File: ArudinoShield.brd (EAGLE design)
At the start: 53.3 x 60.6 mm, 25 parts, among them IC1 L298

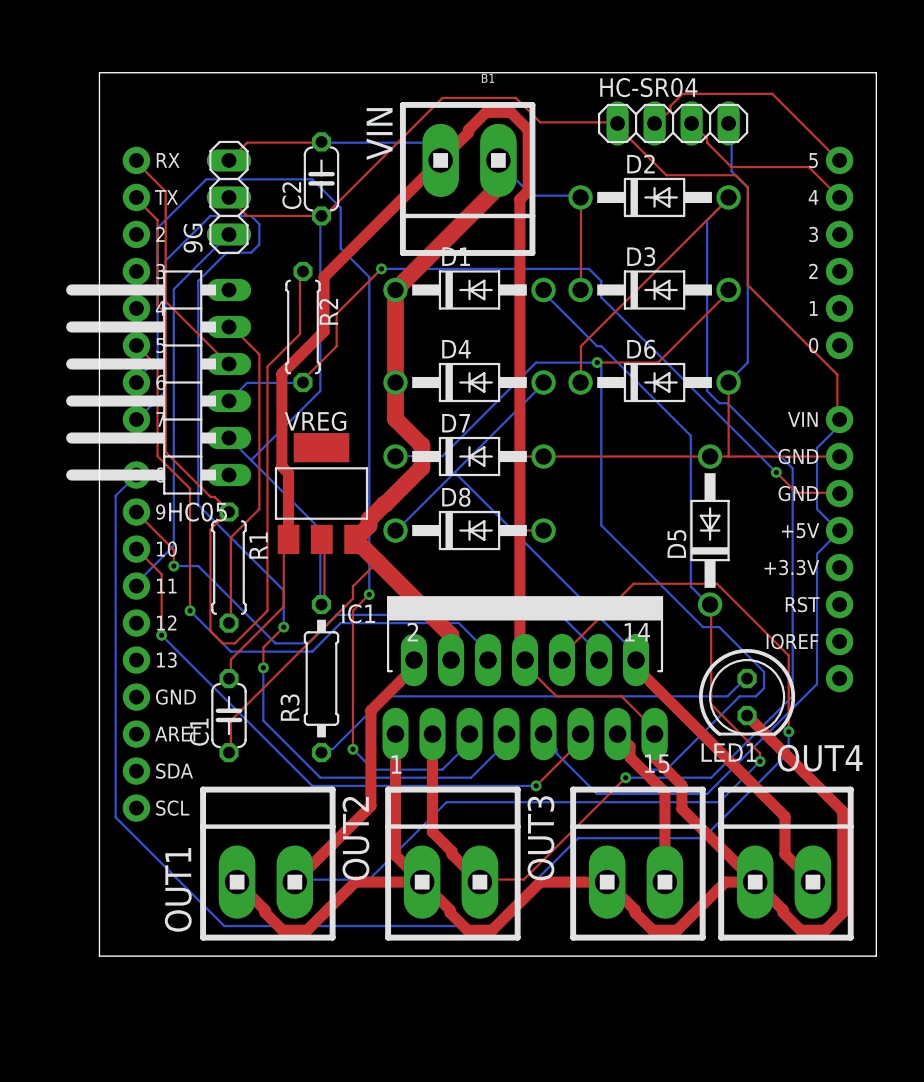
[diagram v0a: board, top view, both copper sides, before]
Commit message: added ground plane, updated layout
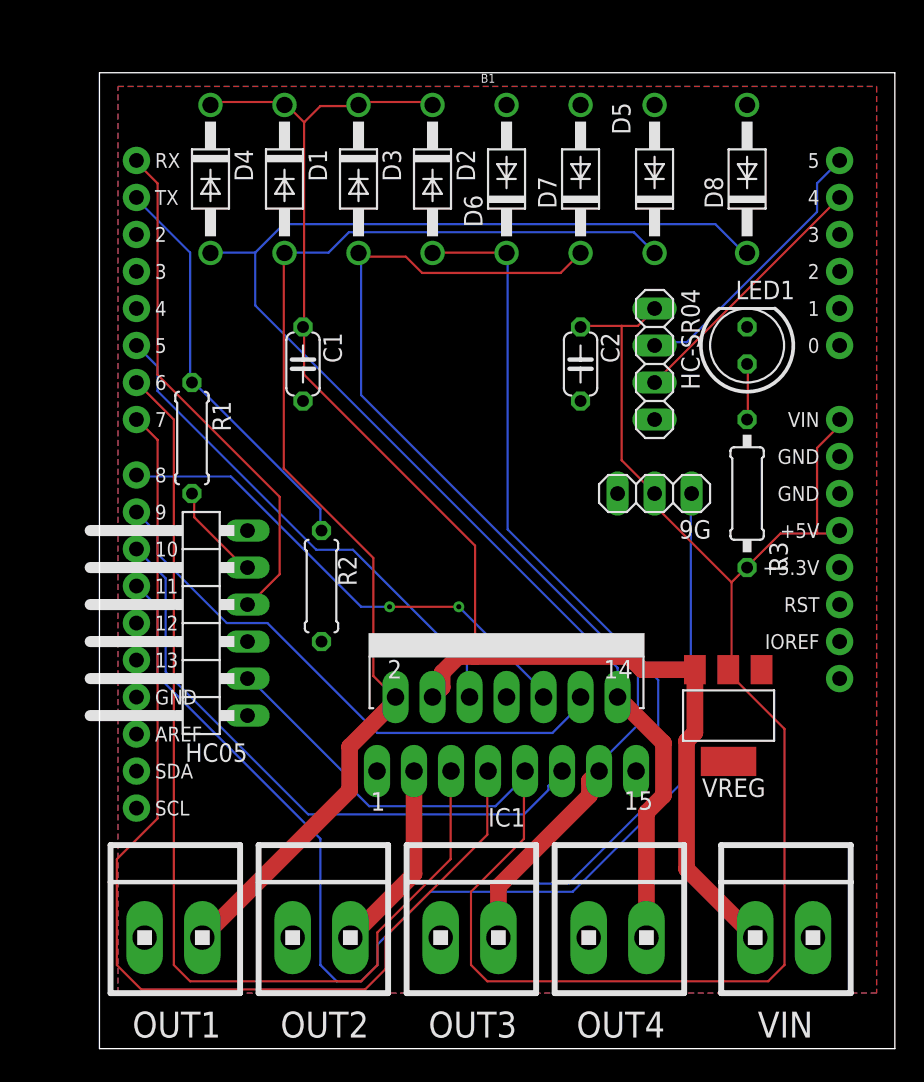
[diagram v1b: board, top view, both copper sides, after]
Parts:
- moved VIN 57.5 mm to (81.3, 20.3), turned to 0 degrees
- moved 9G 35.6 mm to (72.4, 50.8), turned to 180 degrees
- moved R3 31.9 mm to (78.7, 50.8), turned to 270 degrees
- moved VREG 31.8 mm to (77.5, 35.6), turned to 180 degrees
- moved D8 30.7 mm to (78.7, 72.4), turned to 90 degrees
- moved C1 24.7 mm to (48.3, 59.7), turned to 270 degrees
- moved D5 24.4 mm to (72.4, 72.4)
- moved LED1 24.1 mm to (78.7, 61.0), turned to 90 degrees
- moved D4 22.6 mm to (41.9, 72.4), turned to 270 degrees
- moved C2 21.8 mm to (67.3, 59.7), turned to 270 degrees
- moved D3 21.7 mm to (52.1, 72.4), turned to 270 degrees
- moved D7 20.5 mm to (67.3, 72.4), turned to 90 degrees
- moved R2 17.8 mm to (49.5, 44.5)
- moved D6 17.3 mm to (62.2, 72.4), turned to 90 degrees
- moved HC-SR04 16.6 mm to (72.4, 59.7), turned to 270 degrees
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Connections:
- removed net N$13: B1.GND@0, HC05.3, R2.1
- net GND: now also B1.GND@0, HC05.3, R2.1
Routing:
- net GND: track 253.5 -> 0.00 mm
- net IN3: track 104.9 -> 34.6 mm, vias 1 -> 2
- net 9GPWM: track 26.8 -> 83.1 mm
- net N$13: track 54.1 -> 0.00 mm, vias 2 -> 0
- net OUT4: track 52.8 -> 97.6 mm
- net N$11: track 62.6 -> 28.2 mm
- net N$25: track 31.3 -> 3.87 mm
- net VIN: track 73.0 -> 99.0 mm
- net N$12: track 16.6 -> 35.5 mm
- net N$14: track 22.3 -> 6.99 mm
- net OUT1: track 92.7 -> 82.3 mm, vias 1 -> 0
- net +5V: track 142.4 -> 133.5 mm
- net ENA: track 43.5 -> 35.1 mm, vias 1 -> 0
- net OUT2: track 92.7 -> 85.0 mm, vias 1 -> 0
- net ECHO: track 12.4 -> 18.0 mm
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- added copper zone on layer 1, net GND
- added copper zone on layer 16, net GND
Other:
- board size 53.3 x 60.6 mm -> 54.6 x 67 mm

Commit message: updated board and previews
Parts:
- moved R2 15.5 mm to (47.0, 59.7)
- moved R1 5.24 mm to (41.9, 59.7)
- moved C1 3.81 mm to (52.1, 59.7)
- moved 9G 1.27 mm to (72.4, 49.5), turned to 90 degrees
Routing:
- net GND: track 0.00 -> 246.5 mm
- net 9GPWM: track 83.1 -> 38.7 mm
- net OUT3: track 75.3 -> 119.5 mm
- net IN1: track 71.3 -> 47.0 mm, vias 0 -> 1
- net +5V: track 133.5 -> 114.1 mm
- net IN2: track 75.4 -> 89.1 mm, vias 0 -> 1
- net N$11: track 28.2 -> 15.0 mm
- net ENA: track 35.1 -> 44.1 mm
- net OUT2: track 85.0 -> 93.8 mm, vias 0 -> 2
- net OUT4: track 97.6 -> 90.8 mm
- net IN3: track 34.6 -> 39.3 mm, vias 2 -> 1
- net N$14: track 6.99 -> 11.6 mm
- net IN4: track 38.9 -> 36.1 mm, vias 0 -> 1
- net VIN: track 99.0 -> 101.1 mm
- net ENB: track 41.9 -> 43.8 mm, vias 0 -> 1
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
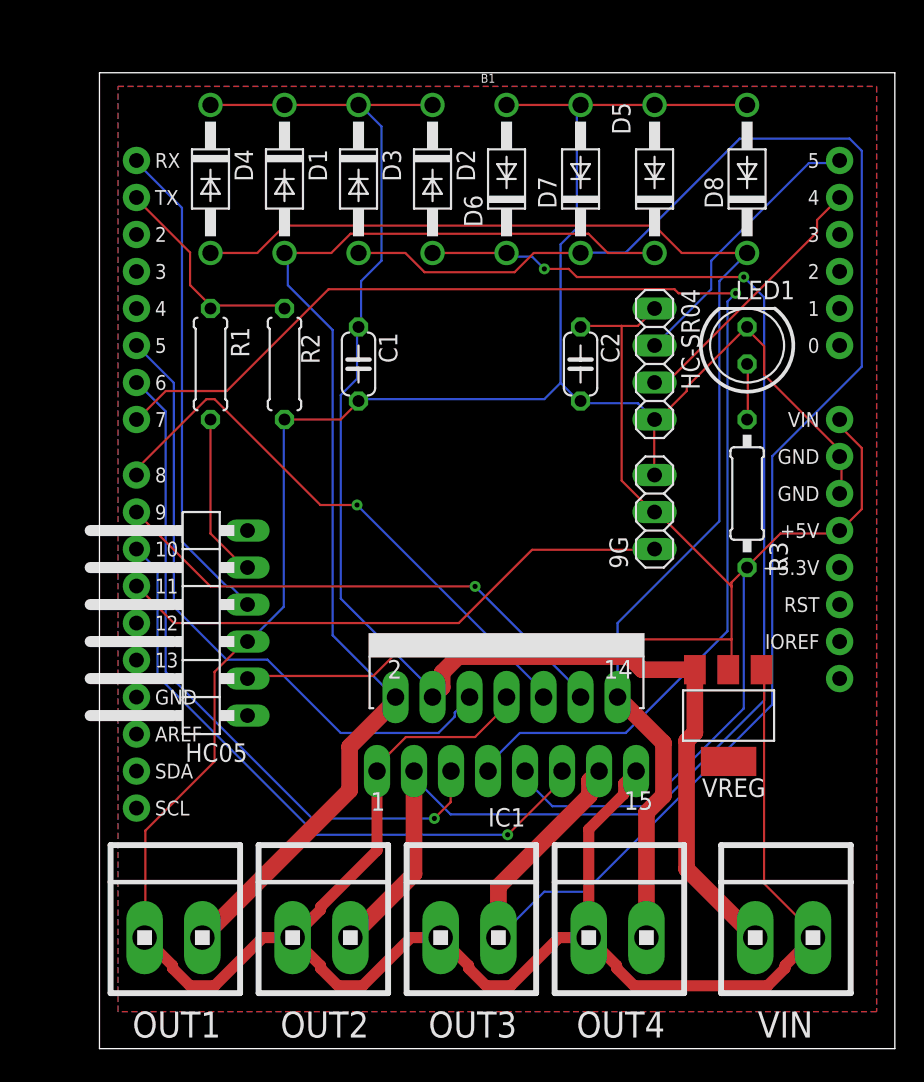
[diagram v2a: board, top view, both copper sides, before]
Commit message: fixed L298 pin 8 not being reliably grounded
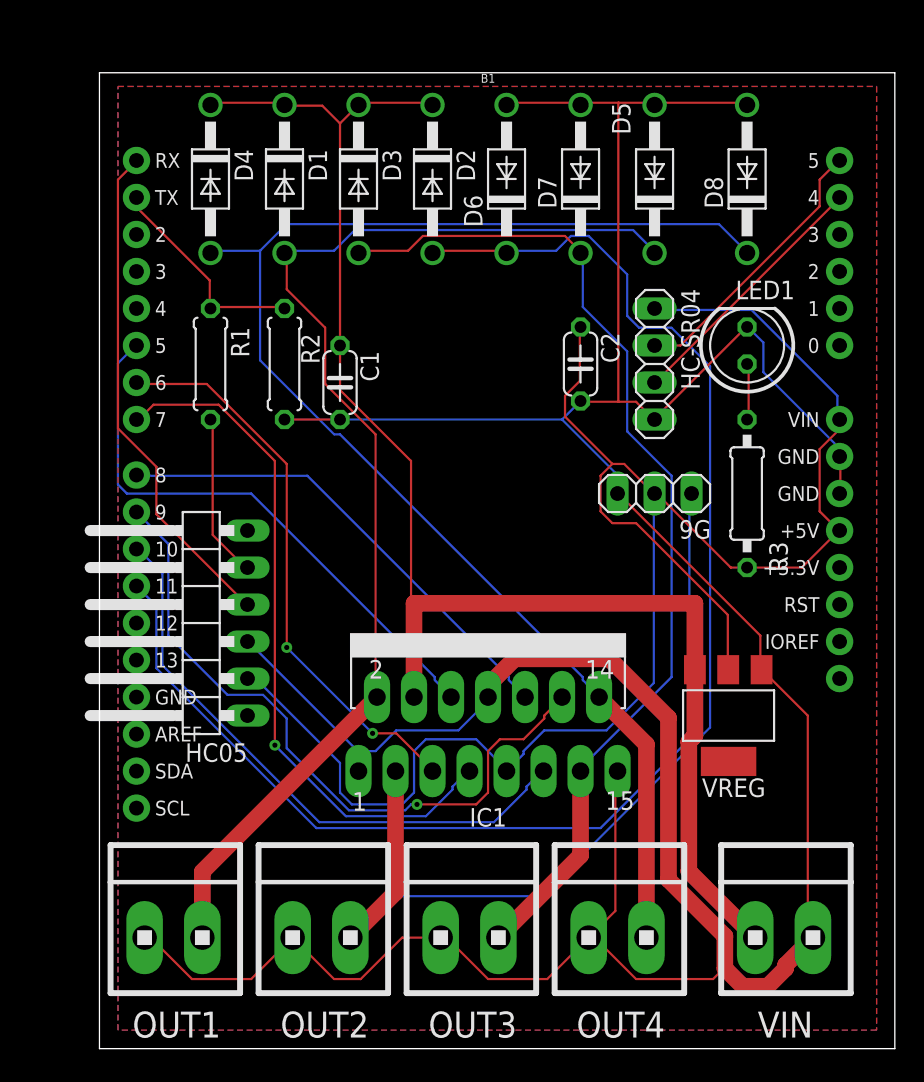
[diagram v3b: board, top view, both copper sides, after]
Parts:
- moved C1 1.80 mm to (50.8, 58.4)
- moved 9G 1.27 mm to (72.4, 50.8), turned to 180 degrees
- moved IC1 1.27 mm to (61.0, 39.4)
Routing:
- net OUT3: track 119.5 -> 70.8 mm
- net IN2: track 89.1 -> 47.8 mm
- net 9GPWM: track 38.7 -> 66.9 mm
- net +5V: track 114.1 -> 128.3 mm
- net IN4: track 36.1 -> 47.6 mm
- net GND: track 246.5 -> 257.0 mm
- net IN1: track 47.0 -> 38.8 mm, vias 1 -> 2
- net IN3: track 39.3 -> 33.1 mm, vias 1 -> 0
- net OUT4: track 90.8 -> 96.8 mm
- net ENA: track 44.1 -> 39.1 mm
- net ENB: track 43.8 -> 40.9 mm, vias 1 -> 0
- net VIN: track 101.1 -> 102.3 mm
- net N$12: track 33.8 -> 34.7 mm
- net OUT1: track 82.2 -> 81.4 mm
- net OUT2: track 93.8 -> 93.2 mm, vias 2 -> 0

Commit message: By hand rework of board layout, no vias
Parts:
- R1: device adafruit:0207/7 -> rcl:0207/10
- R2: value 2K -> 2k; device adafruit:0207/7 -> rcl:0207/10
- moved OUT3 55.8 mm to (71.1, 74.9), turned to 180 degrees
- moved OUT4 55.3 mm to (61.0, 74.9), turned to 180 degrees
- moved D6 45.3 mm to (71.1, 27.9), turned to 0 degrees
- moved D2 43.0 mm to (71.1, 31.8), turned to 180 degrees
- moved LED1 41.1 mm to (72.4, 20.3), turned to 270 degrees
- moved D5 41.0 mm to (61.0, 33.0), turned to 270 degrees
- moved VIN 40.6 mm to (40.6, 20.3)
- moved D1 38.6 mm to (53.3, 34.3), turned to 0 degrees
- moved 9G 32.7 mm to (40.6, 58.4), turned to 270 degrees
- moved C1 29.9 mm to (44.5, 29.2), turned to 0 degrees
- moved HC05 29.5 mm to (36.8, 71.1)
- moved D8 26.5 mm to (53.3, 64.8), turned to 180 degrees
- moved D4 22.5 mm to (48.3, 50.8), turned to 90 degrees
- moved D3 21.7 mm to (72.4, 64.8), turned to 180 degrees
- moved C2 21.6 mm to (68.6, 38.1)
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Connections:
- new net +5VIN: B1.VIN, C2.1, IC1.9, R3.2, VREG.2
- net +5V: no longer B1.VIN, C2.1, IC1.9, R3.2, VREG.2
- net 9GPWM: now also B1.D3; no longer B1.D11
- net ENA: now also B1.D11; no longer B1.D5
- net ENB: now also B1.D9; no longer B1.D10
- net GND: now also VIN.2; no longer VIN.1
- net IN1: now also B1.D12; no longer B1.D6
- net IN2: now also B1.D10; no longer B1.D7
- net IN4: now also B1.D7; no longer B1.D9
- net N$11: now also R1.2; no longer R1.1
- net N$14: now also R1.1; no longer R1.2
- net VIN: now also VIN.1; no longer VIN.2
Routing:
- net GND: track 257.0 -> 14.6 mm
- net OUT4: track 96.8 -> 28.0 mm
- net OUT2: track 93.2 -> 26.9 mm
- net 9GPWM: track 66.9 -> 6.66 mm
- net +5VIN: track 0.00 -> 60.0 mm
- net VIN: track 102.3 -> 148.6 mm
- net OUT1: track 81.4 -> 36.2 mm
- net OUT3: track 70.8 -> 36.9 mm
- net N$12: track 34.7 -> 4.34 mm
- net IN4: track 47.6 -> 22.6 mm, vias 1 -> 0
- net IN2: track 47.8 -> 27.7 mm, vias 1 -> 0
- net ENA: track 39.1 -> 23.2 mm
- net TRIG: track 19.0 -> 5.08 mm
- net ECHO: track 18.1 -> 5.08 mm
- net ENB: track 40.9 -> 28.8 mm
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- removed copper zone on layer 1, net GND

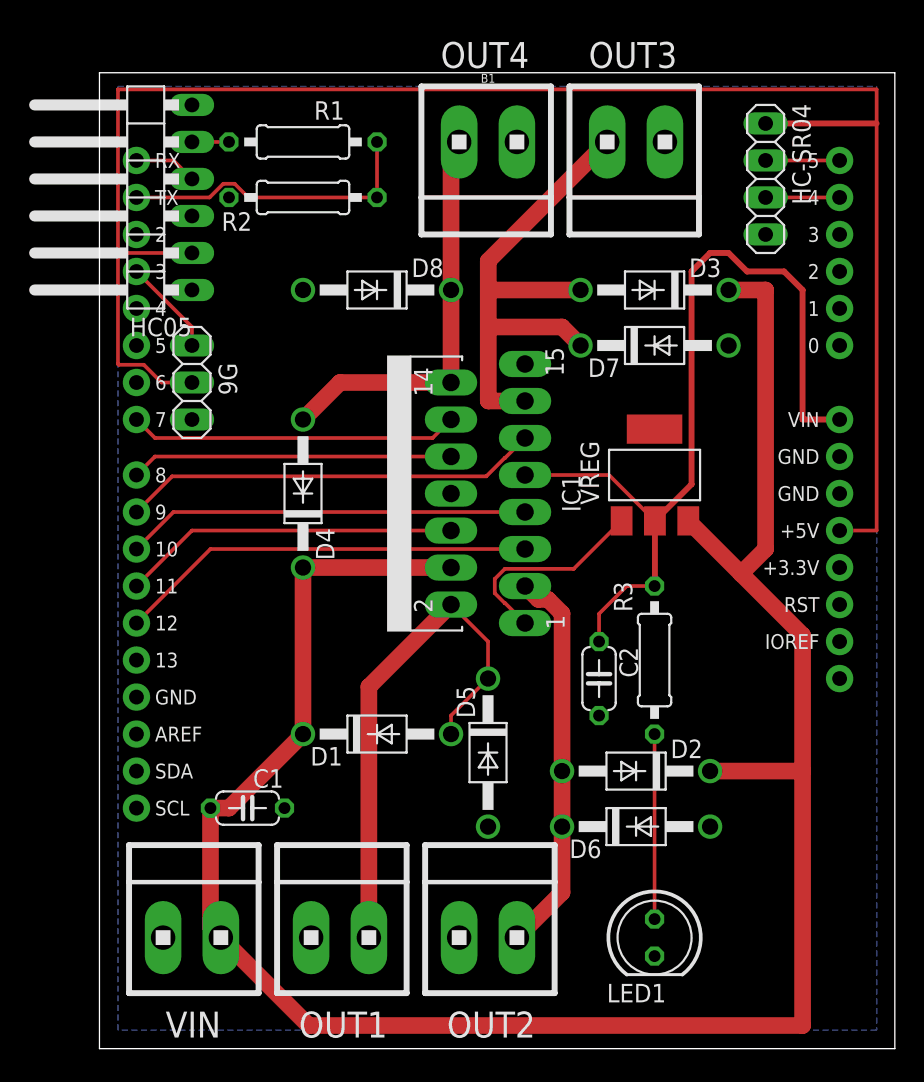
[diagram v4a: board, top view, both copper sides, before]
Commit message: increased minimum trace width
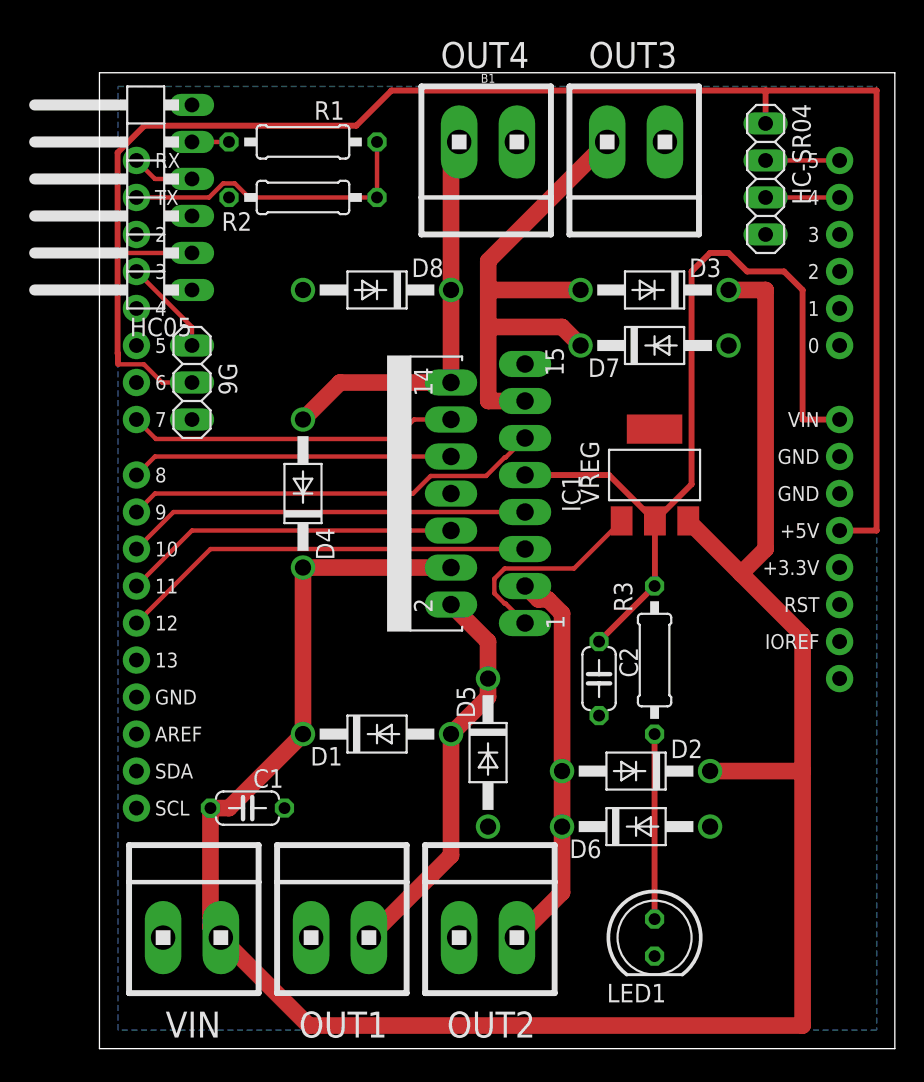
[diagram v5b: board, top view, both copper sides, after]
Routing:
- net OUT1: track 36.2 -> 27.3 mm
- net +5V: track 122.0 -> 114.1 mm
- net +5VIN: track 60.0 -> 58.9 mm

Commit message: minor changes, updated images
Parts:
- moved R1 1.27 mm to (49.5, 74.9)
- moved R2 1.27 mm to (49.5, 71.1)
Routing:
- net N$14: track 2.54 -> 3.81 mm
- net N$11: track 21.1 -> 22.4 mm
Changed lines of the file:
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@@
 <attribute name="VALUE" x="40.64" y="80.645" size="1.27" layer="27" rot="R180"/>
 </element>
-<element name="R2" library="rcl" library_urn="urn:adsk.eagle:library:334" package="0207/10" package3d_urn="urn:adsk.eagle:package:23491/2" value="2k" x="48.26" y="71.12" smashed="yes">
-<attribute name="NAME" x="42.672" y="68.834" size="1.27" layer="25" ratio="10"/>
-<attribute name="POPULARITY" value="36" x="48.26" y="71.12" size="1.778" layer="27" display="off"/>
-<attribute name="SPICEPREFIX" value="R" x="48.26" y="71.12" size="1.778" layer="27" display="off"/>
-<attribute name="VALUE" x="45.9994" y="70.485" size="1.27" layer="27" ratio="10"/>
+<element name="R2" library="rcl" library_urn="urn:adsk.eagle:library:334" package="0207/10" package3d_urn="urn:adsk.eagle:package:23491/2" value="2k" x="49.53" y="71.12" smashed="yes">
+<attribute name="NAME" x="43.942" y="68.834" size="1.27" layer="25" ratio="10"/>
+<attribute name="POPULARITY" value="36" x="49.53" y="71.12" size="1.778" layer="27" display="off"/>
+<attribute name="SPICEPREFIX" value="R" x="49.53" y="71.12" size="1.778" layer="27" display="off"/>
+<attribute name="VALUE" x="47.2694" y="70.485" size="1.27" layer="27" ratio="10"/>
 </element>
-<element name="R1" library="rcl" library_urn="urn:adsk.eagle:library:334" package="0207/10" package3d_urn="urn:adsk.eagle:package:23491/2" value="1k" x="48.26" y="74.93" smashed="yes">
-<attribute name="NAME" x="49.022" y="76.454" size="1.27" layer="25" ratio="10"/>
-<attribute name="POPULARITY" value="36" x="48.26" y="74.93" size="1.778" layer="27" display="off"/>
-<attribute name="SPICEPREFIX" value="R" x="48.26" y="74.93" size="1.778" layer="27" display="off"/>
-<attribute name="VALUE" x="45.9994" y="74.295" size="1.27" layer="27" ratio="10"/>
+<element name="R1" library="rcl" library_urn="urn:adsk.eagle:library:334" package="0207/10" package3d_urn="urn:adsk.eagle:package:23491/2" value="1k" x="49.53" y="74.93" smashed="yes">
+<attribute name="NAME" x="50.292" y="76.454" size="1.27" layer="25" ratio="10"/>
+<attribute name="POPULARITY" value="36" x="49.53" y="74.93" size="1.778" layer="27" display="off"/>
+<attribute name="SPICEPREFIX" value="R" x="49.53" y="74.93" size="1.778" layer="27" display="off"/>
+<attribute name="VALUE" x="47.2694" y="74.295" size="1.27" layer="27" ratio="10"/>
 </element>
 </elements>
@@
 <contactref element="R2" pad="2"/>
 <contactref element="R1" pad="2"/>
-<wire x1="42.7802" y1="72.0852" x2="43.5798" y2="72.0852" width="0.3048" layer="1"/>
-<wire x1="36.83" y1="71.12" x2="41.815" y2="71.12" width="0.3048" layer="1"/>
-<wire x1="44.545" y1="71.12" x2="53.34" y2="71.12" width="0.3048" layer="1"/>
-<wire x1="41.815" y1="71.12" x2="42.7802" y2="72.0852" width="0.3048" layer="1"/>
-<wire x1="43.5798" y1="72.0852" x2="44.545" y2="71.12" width="0.3048" layer="1"/>
-<wire x1="53.34" y1="74.93" x2="53.34" y2="71.12" width="0.3048" layer="1"/>
+<wire x1="44.0502" y1="72.0852" x2="44.8498" y2="72.0852" width="0.3048" layer="1"/>
+<wire x1="36.83" y1="71.12" x2="43.085" y2="71.12" width="0.3048" layer="1"/>
+<wire x1="45.815" y1="71.12" x2="54.61" y2="71.12" width="0.3048" layer="1"/>
+<wire x1="43.085" y1="71.12" x2="44.0502" y2="72.0852" width="0.3048" layer="1"/>
+<wire x1="44.8498" y1="72.0852" x2="45.815" y2="71.12" width="0.3048" layer="1"/>
+<wire x1="54.61" y1="74.93" x2="54.61" y2="71.12" width="0.3048" layer="1"/>
 </signal>
 <signal name="N$14">
 <contactref element="HC05" pad="5"/>
 <contactref element="R1" pad="1"/>
-<wire x1="40.64" y1="74.93" x2="43.18" y2="74.93" width="0.3048" layer="1"/>
+<wire x1="40.64" y1="74.93" x2="44.45" y2="74.93" width="0.3048" layer="1"/>
 </signal>
 <signal name="OUT1">
@@
 <wire x1="87.63" y1="78.4608" x2="80.01" y2="78.4608" width="0.4064" layer="1"/>
 <wire x1="80.01" y1="78.4608" x2="80.01" y2="76.2" width="0.4064" layer="1"/>
-<wire x1="80.01" y1="78.4608" x2="54.3308" y2="78.4608" width="0.4064" layer="1"/>
+<wire x1="80.01" y1="78.4608" x2="45.4408" y2="78.4608" width="0.4064" layer="1"/>
 <wire x1="35.5346" y1="60.423425" x2="35.56" y2="60.398025" width="0.4064" layer="1"/>
 <wire x1="35.56" y1="60.398025" x2="35.56" y2="59.69" width="0.4064" layer="1"/>
 <wire x1="35.5346" y1="74.196575" x2="35.5346" y2="67.31" width="0.4064" layer="1"/>
 <wire x1="35.5346" y1="67.31" x2="35.5346" y2="60.423425" width="0.4064" layer="1"/>
-<wire x1="54.3308" y1="78.4608" x2="51.9176" y2="76.0476" width="0.4064" layer="1"/>
-<wire x1="51.9176" y1="76.0476" x2="37.385625" y2="76.0476" width="0.4064" layer="1"/>
+<wire x1="45.4408" y1="78.4608" x2="43.0276" y2="76.0476" width="0.4064" layer="1"/>
+<wire x1="43.0276" y1="76.0476" x2="37.385625" y2="76.0476" width="0.4064" layer="1"/>
 <wire x1="37.385625" y1="76.0476" x2="35.5346" y2="74.196575" width="0.4064" layer="1"/>
 <wire x1="35.56" y1="59.69" x2="35.5854" y2="59.6646" width="0.3048" layer="1"/>
